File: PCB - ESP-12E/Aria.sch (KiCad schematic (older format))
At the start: 0 parts

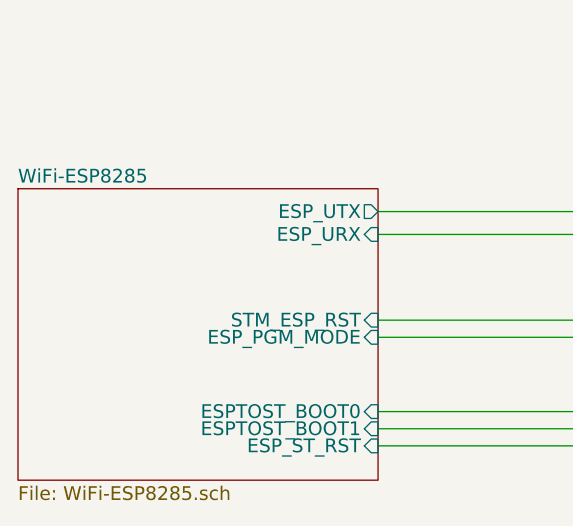
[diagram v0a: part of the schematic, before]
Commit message: DRC Cleared and Pictures
DRC cleared of errors for both Aria board designs. New pictures have
been added. Readme has also been updated.
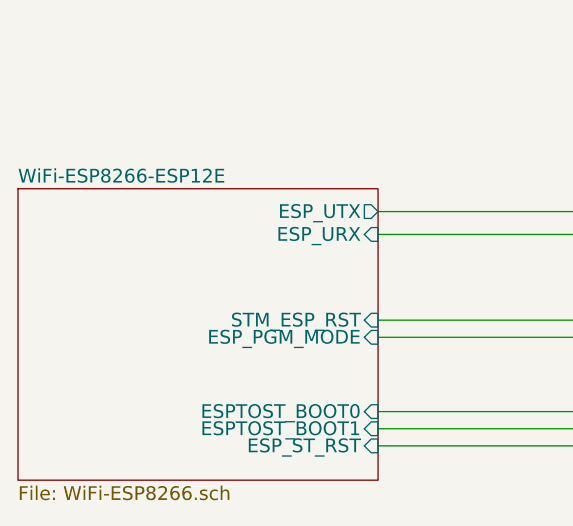
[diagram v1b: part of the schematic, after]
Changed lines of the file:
@@
 S 3250 4100 1575 1275
 U 57E9EAB0
-F0 "WiFi-ESP8285" 60
-F1 "WiFi-ESP8285.sch" 60
+F0 "WiFi-ESP8266-ESP12E" 60
+F1 "WiFi-ESP8266.sch" 60
 F2 "ESP_URX" I R 4825 4300 60
 F3 "ESP_UTX" O R 4825 4200 60

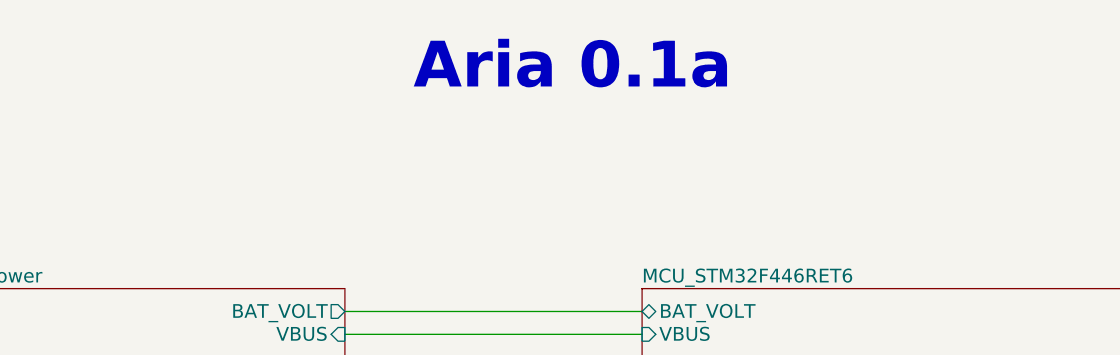
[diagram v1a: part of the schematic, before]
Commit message: Switch
Power switch added for switching board off for storage and shipping.
Power supply circuit routing revised and updated.
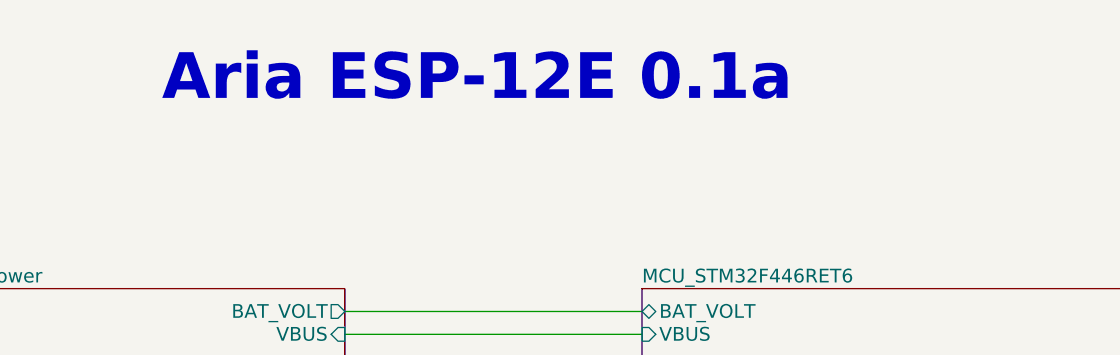
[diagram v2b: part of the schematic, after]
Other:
- note added: "Aria ESP-12E 0.1a"
- note removed: "Aria 0.1a"
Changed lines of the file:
@@
 Wire Wire Line
 	4825 2200 6125 2200
-Text Notes 5125 1150 0    200  ~ 40
-Aria 0.1a
+Text Notes 4025 1200 0    200  ~ 40
+Aria ESP-12E 0.1a
 $Sheet
 S 6125 2000 2650 3375
